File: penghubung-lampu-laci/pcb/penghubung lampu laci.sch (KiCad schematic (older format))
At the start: 8 parts

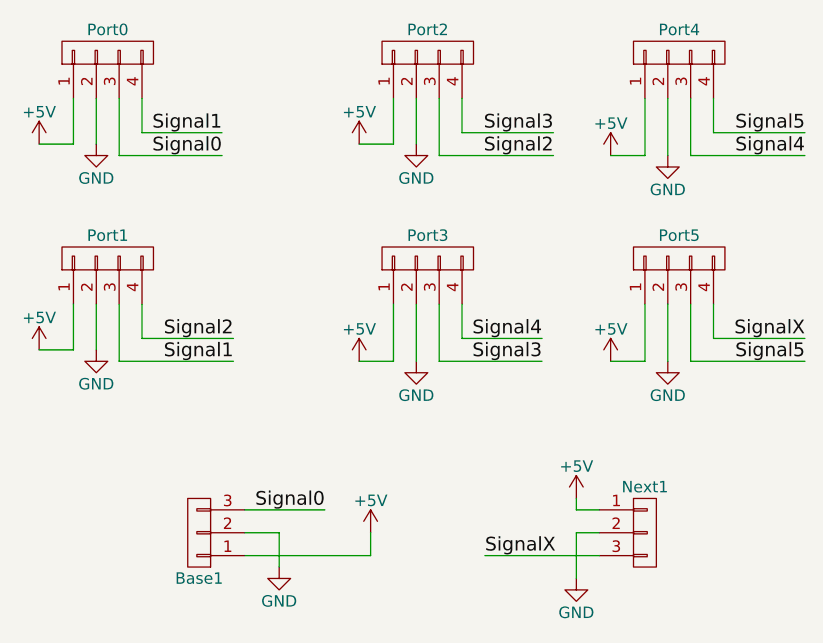
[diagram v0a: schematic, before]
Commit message: Update pin order and component positions
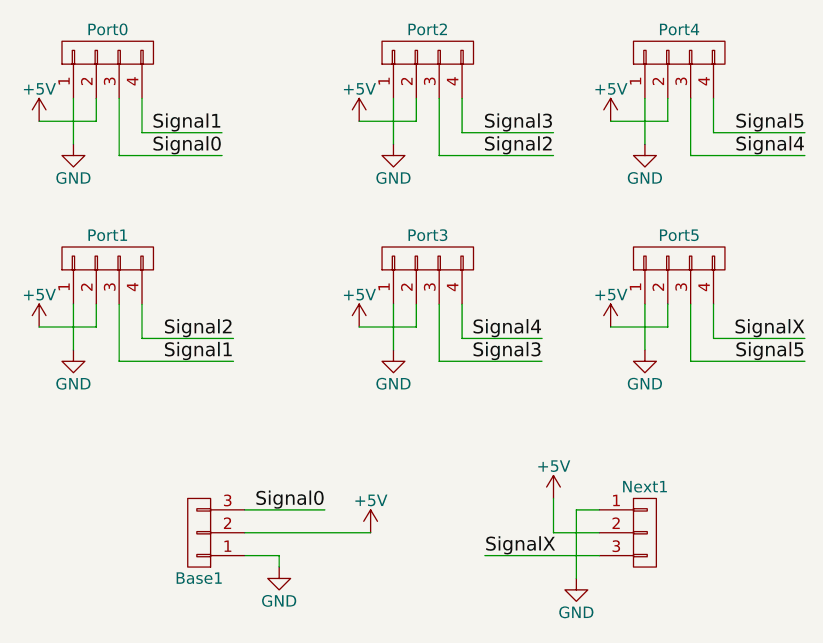
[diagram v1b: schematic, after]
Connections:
- net +5V: now also Base1.2 (P2), Next1.2 (P2), Port0.2 (P2), Port1.2 (P2), Port2.2 (P2), Port3.2 (P2), Port4.2 (P2), Port5.2 (P2); no longer Base1.1 (P1), Next1.1 (P1), Port0.1 (P1), Port1.1 (P1), Port2.1 (P1), Port3.1 (P1), Port4.1 (P1), Port5.1 (P1)
- net GND: now also Base1.1 (P1), Next1.1 (P1), Port0.1 (P1), Port1.1 (P1), Port2.1 (P1), Port3.1 (P1), Port4.1 (P1), Port5.1 (P1); no longer Base1.2 (P2), Next1.2 (P2), Port0.2 (P2), Port1.2 (P2), Port2.2 (P2), Port3.2 (P2), Port4.2 (P2), Port5.2 (P2)
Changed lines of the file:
@@
 L +5V #PWR03
 U 1 1 579E61AE
-P 3050 4300
-F 0 "#PWR03" H 3050 4150 50  0001 C CNN
-F 1 "+5V" H 3050 4440 50  0000 C CNN
-F 2 "" H 3050 4300 50  0000 C CNN
-F 3 "" H 3050 4300 50  0000 C CNN
-	1    3050 4300
+P 2950 4300
+F 0 "#PWR03" H 2950 4150 50  0001 C CNN
+F 1 "+5V" H 2950 4440 50  0000 C CNN
+F 2 "" H 2950 4300 50  0000 C CNN
+F 3 "" H 2950 4300 50  0000 C CNN
+	1    2950 4300
 	1    0    0    -1
 $EndComp
@@
 Text Label 1500 2800 2    60   ~ 0
 Signal0
-Wire Wire Line
-	1600 4550 2150 4550
-Wire Wire Line
-	2150 4550 2150 4450
-Wire Wire Line
-	1600 4450 1750 4450
-Wire Wire Line
-	1750 4450 1750 4600
 $Comp
 L +5V #PWR05
 U 1 1 579E7013
-P 700 2750
-F 0 "#PWR05" H 700 2600 50  0001 C CNN
-F 1 "+5V" H 700 2890 50  0000 C CNN
-F 2 "" H 700 2750 50  0000 C CNN
-F 3 "" H 700 2750 50  0000 C CNN
-	1    700  2750
+P 700 2650
+F 0 "#PWR05" H 700 2500 50  0001 C CNN
+F 1 "+5V" H 700 2790 50  0000 C CNN
+F 2 "" H 700 2650 50  0000 C CNN
+F 3 "" H 700 2650 50  0000 C CNN
+	1    700  2650
 	1    0    0    -1
 $EndComp
@@
 L GND #PWR06
 U 1 1 579E7037
-P 950 2750
-F 0 "#PWR06" H 950 2500 50  0001 C CNN
-F 1 "GND" H 950 2600 50  0000 C CNN
-F 2 "" H 950 2750 50  0000 C CNN
-F 3 "" H 950 2750 50  0000 C CNN
-	1    950  2750
-	1    0    0    -1
-$EndComp
-Wire Wire Line
-	950  2550 950  2750
+P 850 2750
+F 0 "#PWR06" H 850 2500 50  0001 C CNN
+F 1 "GND" H 850 2600 50  0000 C CNN
+F 2 "" H 850 2750 50  0000 C CNN
+F 3 "" H 850 2750 50  0000 C CNN
+	1    850  2750
+	1    0    0    -1
+$EndComp
 Text Label 1500 2700 2    60   ~ 0
 Signal1
 Wire Wire Line
-	850  2550 850  2750
-Wire Wire Line
-	850  2750 700  2750
-Wire Wire Line
 	1500 2700 1150 2700
 Wire Wire Line
@@
 L +5V #PWR07
 U 1 1 579E7C2C
-P 700 3650
-F 0 "#PWR07" H 700 3500 50  0001 C CNN
-F 1 "+5V" H 700 3790 50  0000 C CNN
-F 2 "" H 700 3650 50  0000 C CNN
-F 3 "" H 700 3650 50  0000 C CNN
-	1    700  3650
+P 700 3550
+F 0 "#PWR07" H 700 3400 50  0001 C CNN
+F 1 "+5V" H 700 3690 50  0000 C CNN
+F 2 "" H 700 3550 50  0000 C CNN
+F 3 "" H 700 3550 50  0000 C CNN
+	1    700  3550
 	1    0    0    -1
 $EndComp
@@
 L GND #PWR08
 U 1 1 579E7C4F
-P 950 3650
-F 0 "#PWR08" H 950 3400 50  0001 C CNN
-F 1 "GND" H 950 3500 50  0000 C CNN
-F 2 "" H 950 3650 50  0000 C CNN
-F 3 "" H 950 3650 50  0000 C CNN
-	1    950  3650
+P 850 3650
+F 0 "#PWR08" H 850 3400 50  0001 C CNN
+F 1 "GND" H 850 3500 50  0000 C CNN
+F 2 "" H 850 3650 50  0000 C CNN
+F 3 "" H 850 3650 50  0000 C CNN
+	1    850  3650
 	1    0    0    -1
 $EndComp
@@
 Signal1
 Wire Wire Line
-	850  3450 850  3650
-Wire Wire Line
-	850  3650 700  3650
-Wire Wire Line
-	950  3450 950  3650
-Wire Wire Line
 	1050 3450 1050 3700
 Wire Wire Line
@@
 L +5V #PWR09
 U 1 1 579E821D
-P 2100 2750
-F 0 "#PWR09" H 2100 2600 50  0001 C CNN
-F 1 "+5V" H 2100 2890 50  0000 C CNN
-F 2 "" H 2100 2750 50  0000 C CNN
-F 3 "" H 2100 2750 50  0000 C CNN
-	1    2100 2750
+P 2100 2650
+F 0 "#PWR09" H 2100 2500 50  0001 C CNN
+F 1 "+5V" H 2100 2790 50  0000 C CNN
+F 2 "" H 2100 2650 50  0000 C CNN
+F 3 "" H 2100 2650 50  0000 C CNN
+	1    2100 2650
 	1    0    0    -1
 $EndComp
@@
 L GND #PWR010
 U 1 1 579E8240
-P 2350 2750
-F 0 "#PWR010" H 2350 2500 50  0001 C CNN
-F 1 "GND" H 2350 2600 50  0000 C CNN
-F 2 "" H 2350 2750 50  0000 C CNN
-F 3 "" H 2350 2750 50  0000 C CNN
-	1    2350 2750
+P 2250 2750
+F 0 "#PWR010" H 2250 2500 50  0001 C CNN
+F 1 "GND" H 2250 2600 50  0000 C CNN
+F 2 "" H 2250 2750 50  0000 C CNN
+F 3 "" H 2250 2750 50  0000 C CNN
+	1    2250 2750
 	1    0    0    -1
 $EndComp
@@
 L +5V #PWR011
 U 1 1 579E8345
-P 2100 3700
-F 0 "#PWR011" H 2100 3550 50  0001 C CNN
-F 1 "+5V" H 2100 3840 50  0000 C CNN
-F 2 "" H 2100 3700 50  0000 C CNN
-F 3 "" H 2100 3700 50  0000 C CNN
-	1    2100 3700
+P 2100 3550
+F 0 "#PWR011" H 2100 3400 50  0001 C CNN
+F 1 "+5V" H 2100 3690 50  0000 C CNN
+F 2 "" H 2100 3550 50  0000 C CNN
+F 3 "" H 2100 3550 50  0000 C CNN
+	1    2100 3550
 	1    0    0    -1
 $EndComp
@@
 L GND #PWR012
 U 1 1 579E8368
-P 2350 3700
-F 0 "#PWR012" H 2350 3450 50  0001 C CNN
-F 1 "GND" H 2350 3550 50  0000 C CNN
-F 2 "" H 2350 3700 50  0000 C CNN
-F 3 "" H 2350 3700 50  0000 C CNN
-	1    2350 3700
+P 2250 3650
+F 0 "#PWR012" H 2250 3400 50  0001 C CNN
+F 1 "GND" H 2250 3500 50  0000 C CNN
+F 2 "" H 2250 3650 50  0000 C CNN
+F 3 "" H 2250 3650 50  0000 C CNN
+	1    2250 3650
 	1    0    0    -1
 $EndComp
@@
 L +5V #PWR013
 U 1 1 579E84A1
-P 3200 2800
-F 0 "#PWR013" H 3200 2650 50  0001 C CNN
-F 1 "+5V" H 3200 2940 50  0000 C CNN
-F 2 "" H 3200 2800 50  0000 C CNN
-F 3 "" H 3200 2800 50  0000 C CNN
-	1    3200 2800
+P 3200 2650
+F 0 "#PWR013" H 3200 2500 50  0001 C CNN
+F 1 "+5V" H 3200 2790 50  0000 C CNN
+F 2 "" H 3200 2650 50  0000 C CNN
+F 3 "" H 3200 2650 50  0000 C CNN
+	1    3200 2650
 	1    0    0    -1
 $EndComp
@@
 L GND #PWR014
 U 1 1 579E84E6
-P 3450 2800
-F 0 "#PWR014" H 3450 2550 50  0001 C CNN
-F 1 "GND" H 3450 2650 50  0000 C CNN
-F 2 "" H 3450 2800 50  0000 C CNN
-F 3 "" H 3450 2800 50  0000 C CNN
-	1    3450 2800
+P 3350 2750
+F 0 "#PWR014" H 3350 2500 50  0001 C CNN
+F 1 "GND" H 3350 2600 50  0000 C CNN
+F 2 "" H 3350 2750 50  0000 C CNN
+F 3 "" H 3350 2750 50  0000 C CNN
+	1    3350 2750
 	1    0    0    -1
 $EndComp
@@
 L +5V #PWR015
 U 1 1 579E85DB
-P 3200 3700
-F 0 "#PWR015" H 3200 3550 50  0001 C CNN
-F 1 "+5V" H 3200 3840 50  0000 C CNN
-F 2 "" H 3200 3700 50  0000 C CNN
-F 3 "" H 3200 3700 50  0000 C CNN
-	1    3200 3700
+P 3200 3550
+F 0 "#PWR015" H 3200 3400 50  0001 C CNN
+F 1 "+5V" H 3200 3690 50  0000 C CNN
+F 2 "" H 3200 3550 50  0000 C CNN
+F 3 "" H 3200 3550 50  0000 C CNN
+	1    3200 3550
 	1    0    0    -1
 $EndComp
@@
 L GND #PWR016
 U 1 1 579E85FE
-P 3450 3700
-F 0 "#PWR016" H 3450 3450 50  0001 C CNN
-F 1 "GND" H 3450 3550 50  0000 C CNN
-F 2 "" H 3450 3700 50  0000 C CNN
-F 3 "" H 3450 3700 50  0000 C CNN
-	1    3450 3700
+P 3350 3650
+F 0 "#PWR016" H 3350 3400 50  0001 C CNN
+F 1 "GND" H 3350 3500 50  0000 C CNN
+F 2 "" H 3350 3650 50  0000 C CNN
+F 3 "" H 3350 3650 50  0000 C CNN
+	1    3350 3650
 	1    0    0    -1
 $EndComp
@@
 SignalX
 Wire Wire Line
-	2100 2750 2250 2750
-Wire Wire Line
-	2250 2750 2250 2550
-Wire Wire Line
-	2350 2550 2350 2750
-Wire Wire Line
 	2450 2550 2450 2800
 Wire Wire Line
@@
 	2450 3700 2450 3450
 Wire Wire Line
-	2350 3700 2350 3450
-Wire Wire Line
-	2100 3700 2250 3700
-Wire Wire Line
-	2250 3700 2250 3450
-Wire Wire Line
-	3200 2800 3350 2800
-Wire Wire Line
-	3350 2800 3350 2550
-Wire Wire Line
-	3450 2550 3450 2800
-Wire Wire Line
 	4050 2800 3550 2800
 Wire Wire Line
@@
 	3650 2700 3650 2550
 Wire Wire Line
-	3200 3700 3350 3700
-Wire Wire Line
-	3350 3700 3350 3450
-Wire Wire Line
-	3450 3450 3450 3700
-Wire Wire Line
 	4050 3700 3550 3700
 Wire Wire Line
@@
 	3650 3600 3650 3450
 Wire Wire Line
+	2650 4550 3150 4550
+Wire Wire Line
+	1600 4550 1750 4550
+Wire Wire Line
+	1750 4550 1750 4600
+Wire Wire Line
+	1600 4450 2150 4450
+Wire Wire Line
 	3150 4350 3050 4350
 Wire Wire Line
-	3050 4350 3050 4300
-Wire Wire Line
-	3050 4650 3050 4450
-Wire Wire Line
-	3050 4450 3150 4450
-Wire Wire Line
-	2650 4550 3150 4550
+	3050 4350 3050 4650
+Wire Wire Line
+	3150 4450 2950 4450
+Wire Wire Line
+	2950 4450 2950 4300
+Wire Wire Line
+	3200 3550 3450 3550
+Wire Wire Line
+	3450 3550 3450 3450
+Wire Wire Line
+	3350 3450 3350 3650
+Wire Wire Line
+	3350 2550 3350 2750
+Wire Wire Line
+	3200 2650 3450 2650
+Wire Wire Line
+	3450 2650 3450 2550
+Wire Wire Line
+	2100 2650 2350 2650
+Wire Wire Line
+	2350 2650 2350 2550
+Wire Wire Line
+	2250 2550 2250 2750
+Wire Wire Line
+	2100 3550 2350 3550
+Wire Wire Line
+	2350 3550 2350 3450
+Wire Wire Line
+	2250 3450 2250 3650
+Wire Wire Line
+	700  3550 950  3550
+Wire Wire Line
+	950  3550 950  3450
+Wire Wire Line
+	850  3450 850  3650
+Wire Wire Line
+	700  2650 950  2650
+Wire Wire Line
+	950  2650 950  2550
+Wire Wire Line
+	850  2550 850  2750
 $EndSCHEMATC
